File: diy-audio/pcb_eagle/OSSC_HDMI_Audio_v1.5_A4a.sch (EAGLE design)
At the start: 29 parts, among them U1 PCM1808, U2 74LVC1G34, U3 MK2507SLF

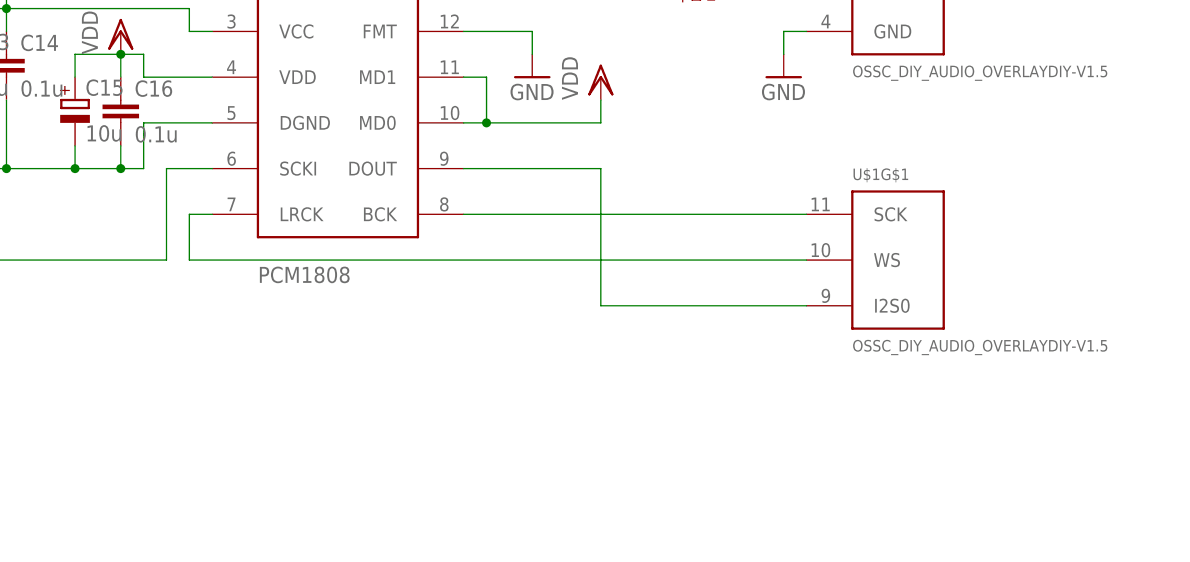
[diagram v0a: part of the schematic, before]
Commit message: PCB files with a pad for mclk to IT6613E
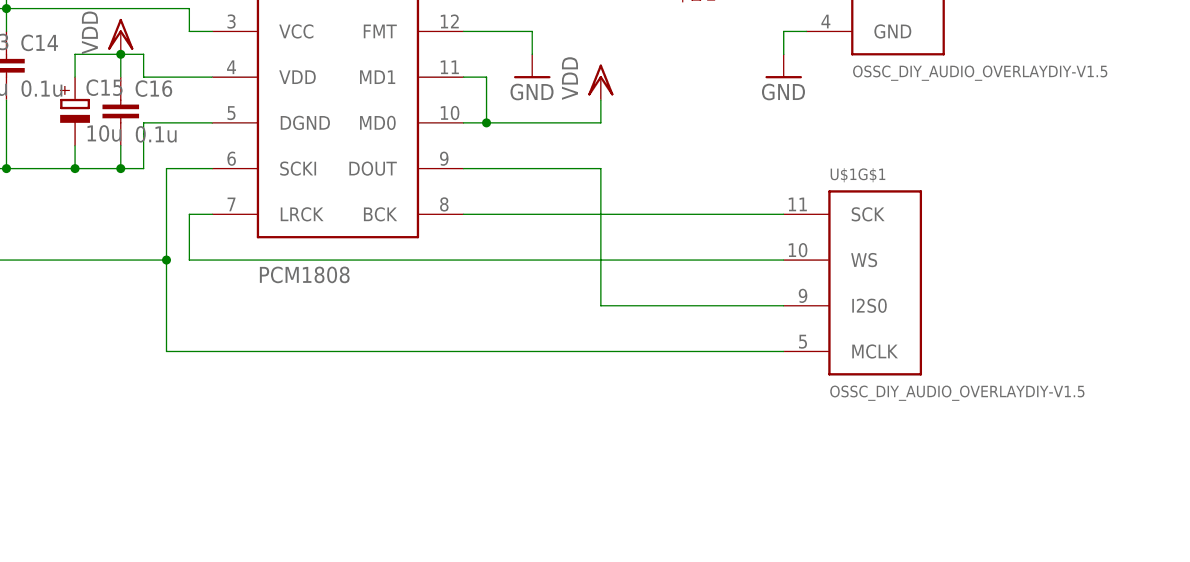
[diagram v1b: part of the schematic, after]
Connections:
- net N$17: now also U$1G$1.MCLK
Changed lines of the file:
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@@
 <?xml version="1.0" encoding="utf-8"?>
 <!DOCTYPE eagle SYSTEM "eagle.dtd">
-<eagle version="6.6.0">
+<eagle version="7.6.0">
 <drawing>
 <settings>
@@
 <grid distance="0.1" unitdist="inch" unit="inch" style="lines" multiple="1" display="no" altdistance="0.01" altunitdist="inch" altunit="inch"/>
 <layers>
-<layer number="1" name="Top" color="4" fill="1" visible="yes" active="no"/>
-<layer number="16" name="Bottom" color="1" fill="1" visible="yes" active="no"/>
-<layer number="17" name="Pads" color="2" fill="1" visible="yes" active="no"/>
-<layer number="18" name="Vias" color="2" fill="1" visible="yes" active="no"/>
-<layer number="19" name="Unrouted" color="6" fill="1" visible="yes" active="no"/>
-<layer number="20" name="Dimension" color="15" fill="1" visible="yes" active="no"/>
-<layer number="21" name="tPlace" color="7" fill="1" visible="yes" active="no"/>
-<layer number="22" name="bPlace" color="7" fill="1" visible="yes" active="no"/>
-<layer number="23" name="tOrigins" color="15" fill="1" visible="yes" active="no"/>
-<layer number="24" name="bOrigins" color="15" fill="1" visible="yes" active="no"/>
-<layer number="25" name="tNames" color="7" fill="1" visible="yes" active="no"/>
-<layer number="26" name="bNames" color="7" fill="1" visible="yes" active="no"/>
-<layer number="27" name="tValues" color="7" fill="1" visible="yes" active="no"/>
-<layer number="28" name="bValues" color="7" fill="1" visible="yes" active="no"/>
+<layer number="1" name="Top" color="4" fill="1" visible="no" active="no"/>
+<layer number="16" name="Bottom" color="1" fill="1" visible="no" active="no"/>
+<layer number="17" name="Pads" color="2" fill="1" visible="no" active="no"/>
+<layer number="18" name="Vias" color="2" fill="1" visible="no" active="no"/>
+<layer number="19" name="Unrouted" color="6" fill="1" visible="no" active="no"/>
+<layer number="20" name="Dimension" color="15" fill="1" visible="no" active="no"/>
+<layer number="21" name="tPlace" color="7" fill="1" visible="no" active="no"/>
+<layer number="22" name="bPlace" color="7" fill="1" visible="no" active="no"/>
+<layer number="23" name="tOrigins" color="15" fill="1" visible="no" active="no"/>
+<layer number="24" name="bOrigins" color="15" fill="1" visible="no" active="no"/>
+<layer number="25" name="tNames" color="7" fill="1" visible="no" active="no"/>
+<layer number="26" name="bNames" color="7" fill="1" visible="no" active="no"/>
+<layer number="27" name="tValues" color="7" fill="1" visible="no" active="no"/>
+<layer number="28" name="bValues" color="7" fill="1" visible="no" active="no"/>
 <layer number="29" name="tStop" color="7" fill="3" visible="no" active="no"/>
 <layer number="30" name="bStop" color="7" fill="6" visible="no" active="no"/>
@@
 <layer number="35" name="tGlue" color="7" fill="4" visible="no" active="no"/>
 <layer number="36" name="bGlue" color="7" fill="5" visible="no" active="no"/>
-<layer number="37" name="tTest" color="7" fill="1" visible="yes" active="no"/>
-<layer number="38" name="bTest" color="7" fill="1" visible="yes" active="no"/>
+<layer number="37" name="tTest" color="7" fill="1" visible="no" active="no"/>
+<layer number="38" name="bTest" color="7" fill="1" visible="no" active="no"/>
 <layer number="39" name="tKeepout" color="4" fill="11" visible="no" active="no"/>
 <layer number="40" name="bKeepout" color="1" fill="11" visible="no" active="no"/>
@@
 <layer number="44" name="Drills" color="7" fill="1" visible="no" active="no"/>
 <layer number="45" name="Holes" color="7" fill="1" visible="no" active="no"/>
-<layer number="46" name="Milling" color="3" fill="1" visible="yes" active="no"/>
-<layer number="47" name="Measures" color="7" fill="1" visible="yes" active="no"/>
-<layer number="48" name="Document" color="7" fill="1" visible="yes" active="no"/>
-<layer number="49" name="Reference" color="7" fill="1" visible="yes" active="no"/>
-<layer number="51" name="tDocu" color="7" fill="1" visible="yes" active="no"/>
-<layer number="52" name="bDocu" color="7" fill="1" visible="yes" active="no"/>
+<layer number="46" name="Milling" color="3" fill="1" visible="no" active="no"/>
+<layer number="47" name="Measures" color="7" fill="1" visible="no" active="no"/>
+<layer number="48" name="Document" color="7" fill="1" visible="no" active="no"/>
+<layer number="49" name="Reference" color="7" fill="1" visible="no" active="no"/>
+<layer number="51" name="tDocu" color="7" fill="1" visible="no" active="no"/>
+<layer number="52" name="bDocu" color="7" fill="1" visible="no" active="no"/>
 <layer number="90" name="Modules" color="5" fill="1" visible="yes" active="yes"/>
 <layer number="91" name="Nets" color="2" fill="1" visible="yes" active="yes"/>
@@
 <part name="FB2" library="rcl" deviceset="R-EU_" device="R0603"/>
 <part name="U2" library="OSSC_HDMI_Audio" deviceset="74LVC1G34" device=""/>
-<part name="U$1" library="OSSC_HDMI_Audio" deviceset="OSSC_DIY_AUDIO_OVERLAY" device="DIY-V1.5"/>
+<part name="U$1" library="OSSC_HDMI_Audio" deviceset="OSSC_DIY_AUDIO_OVERLAY" device="DIY-V1.5" value="OSSC_DIY_AUDIO_OVERLAYDIY-V1.5"/>
 </parts>
 <sheets>
@@
 <instance part="U2" gate="G$1" x="22.86" y="30.48"/>
 <instance part="U2" gate="G$2" x="83.82" y="48.26"/>
-<instance part="U$1" gate="G$1" x="205.74" y="22.86"/>
+<instance part="U$1" gate="G$1" x="205.74" y="27.94"/>
 <instance part="U$1" gate="G$2" x="208.28" y="60.96"/>
 </instances>
@@
 <wire x1="134.62" y1="35.56" x2="132.08" y2="35.56" width="0.1524" layer="91"/>
 <wire x1="132.08" y1="35.56" x2="132.08" y2="30.48" width="0.1524" layer="91"/>
-<wire x1="132.08" y1="30.48" x2="200.66" y2="30.48" width="0.1524" layer="91"/>
+<wire x1="132.08" y1="30.48" x2="198.12" y2="30.48" width="0.1524" layer="91"/>
 <pinref part="U$1" gate="G$1" pin="WS"/>
 </segment>
@@
 <net name="N$14" class="0">
 <segment>
-<wire x1="162.56" y1="35.56" x2="200.66" y2="35.56" width="0.1524" layer="91"/>
+<wire x1="162.56" y1="35.56" x2="198.12" y2="35.56" width="0.1524" layer="91"/>
 <pinref part="U1" gate="G$1" pin="BCK"/>
 <pinref part="U$1" gate="G$1" pin="SCK"/>
@@
 <wire x1="162.56" y1="40.64" x2="177.8" y2="40.64" width="0.1524" layer="91"/>
 <wire x1="177.8" y1="40.64" x2="177.8" y2="25.4" width="0.1524" layer="91"/>
-<wire x1="177.8" y1="25.4" x2="200.66" y2="25.4" width="0.1524" layer="91"/>
+<wire x1="177.8" y1="25.4" x2="198.12" y2="25.4" width="0.1524" layer="91"/>
 <pinref part="U$1" gate="G$1" pin="I2S0"/>
 </segment>
@@
 <pinref part="R31" gate="G$1" pin="2"/>
 <wire x1="129.54" y1="30.48" x2="91.44" y2="30.48" width="0.1524" layer="91"/>
-</segment>
-</net>
+<pinref part="U$1" gate="G$1" pin="MCLK"/>
+<wire x1="198.12" y1="20.32" x2="129.54" y2="20.32" width="0.1524" layer="91"/>
+<wire x1="129.54" y1="20.32" x2="129.54" y2="30.48" width="0.1524" layer="91"/>
+<junction x="129.54" y="30.48"/>
+</segment>
+</net>
